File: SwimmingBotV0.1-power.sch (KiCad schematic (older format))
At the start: 17 parts, among them U1 LT3470A, U10 TPS6216X

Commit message: hoh, working on power stuffs now
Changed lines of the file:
@@
 $Descr A4 11693 8268
 encoding utf-8
-Sheet 3 8
+Sheet 2 8
 Title ""
 Date ""
@@
 P 7850 3950
 F 0 "L1" V 7800 3950 50  0000 C CNN
-F 1 "10uH Isat 400mA" V 7950 3950 50  0000 C CNN
+F 1 "10uH Isat 400mA" V 7800 4400 50  0000 C CNN
 F 2 "Resistors_SMD:R_1210" H 7850 3950 50  0001 C CNN
 F 3 "" H 7850 3950 50  0000 C CNN
@@
 P 7500 4150
 F 0 "C40" H 7400 4250 50  0000 L CNN
-F 1 "100nF" H 7525 4050 50  0000 L CNN
+F 1 "100nF" H 7300 4050 50  0000 L CNN
 F 2 "Capacitors_SMD:C_0402" H 7538 4000 50  0001 C CNN
 F 3 "" H 7500 4150 50  0000 C CNN

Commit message: not final, moving towards board v0.2
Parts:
- added R?: 10k, Resistors_SMD:R_0402, symbol R
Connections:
- net 1S: now also R?.1
- net PROC_3.3V_EN: now also R?.2
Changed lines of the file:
@@
 $EndComp
-Wire Wire Line
-	6150 4200 6050 4200
-Wire Wire Line
-	6050 4200 6050 3850
-Connection ~ 6050 3850
 Wire Wire Line
 	6150 4100 5950 4100
@@
 	5950 4100 5950 5000
 Connection ~ 5950 5000
-Wire Wire Line
-	6150 4400 6100 4400
-Text HLabel 6100 4400 0    60   Input ~ 0
+Text HLabel 6000 4600 0    60   Input ~ 0
 PROC_3.3V_EN
 $Comp
@@
 $EndComp
 Wire Wire Line
-	6700 1800 5850 1800
+	5850 1800 6700 1800
 Wire Wire Line
 	6450 2100 5850 2100
@@
 	1    0    0    -1
 $EndComp
+$Comp
+L R R?
+U 1 1 57477723
+P 6300 4600
+F 0 "R?" V 6380 4600 50  0000 C CNN
+F 1 "10k" V 6300 4600 50  0000 C CNN
+F 2 "Resistors_SMD:R_0402" V 6230 4600 50  0001 C CNN
+F 3 "" H 6300 4600 50  0000 C CNN
+	1    6300 4600
+	0    1    1    0
+$EndComp
+Wire Wire Line
+	6150 4600 6150 4400
+Text Label 6450 4600 0    60   ~ 0
+1S
+Wire Wire Line
+	6000 4600 6150 4600
+Connection ~ 6150 4600
+Wire Wire Line
+	6150 4200 6050 4200
+Wire Wire Line
+	6050 4200 6050 3850
 $EndSCHEMATC

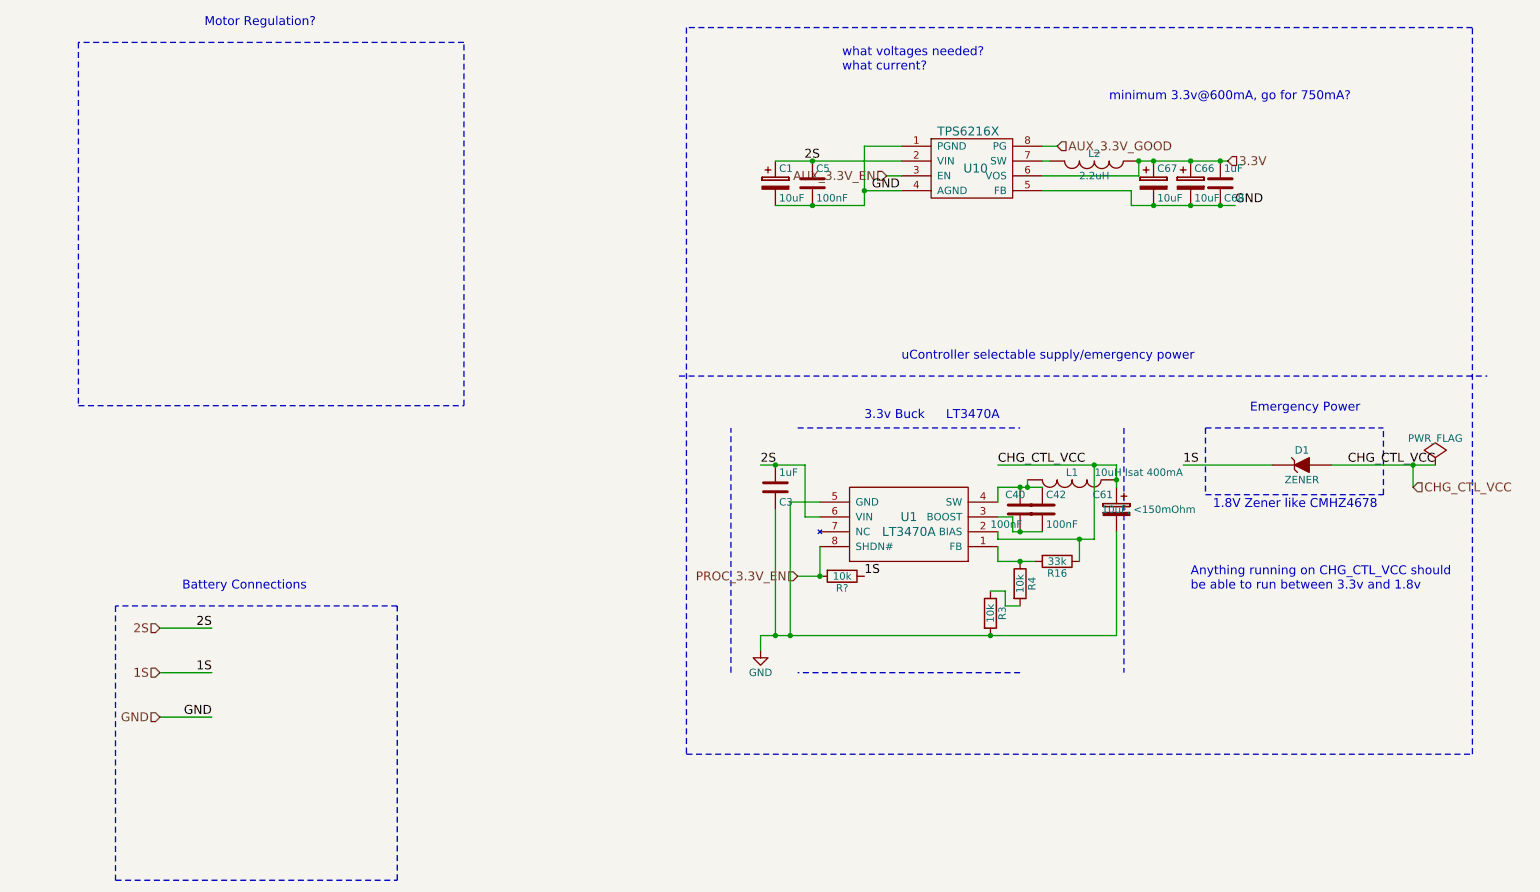
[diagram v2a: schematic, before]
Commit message: potentially done with parts removal and reselection, on to pcb layout
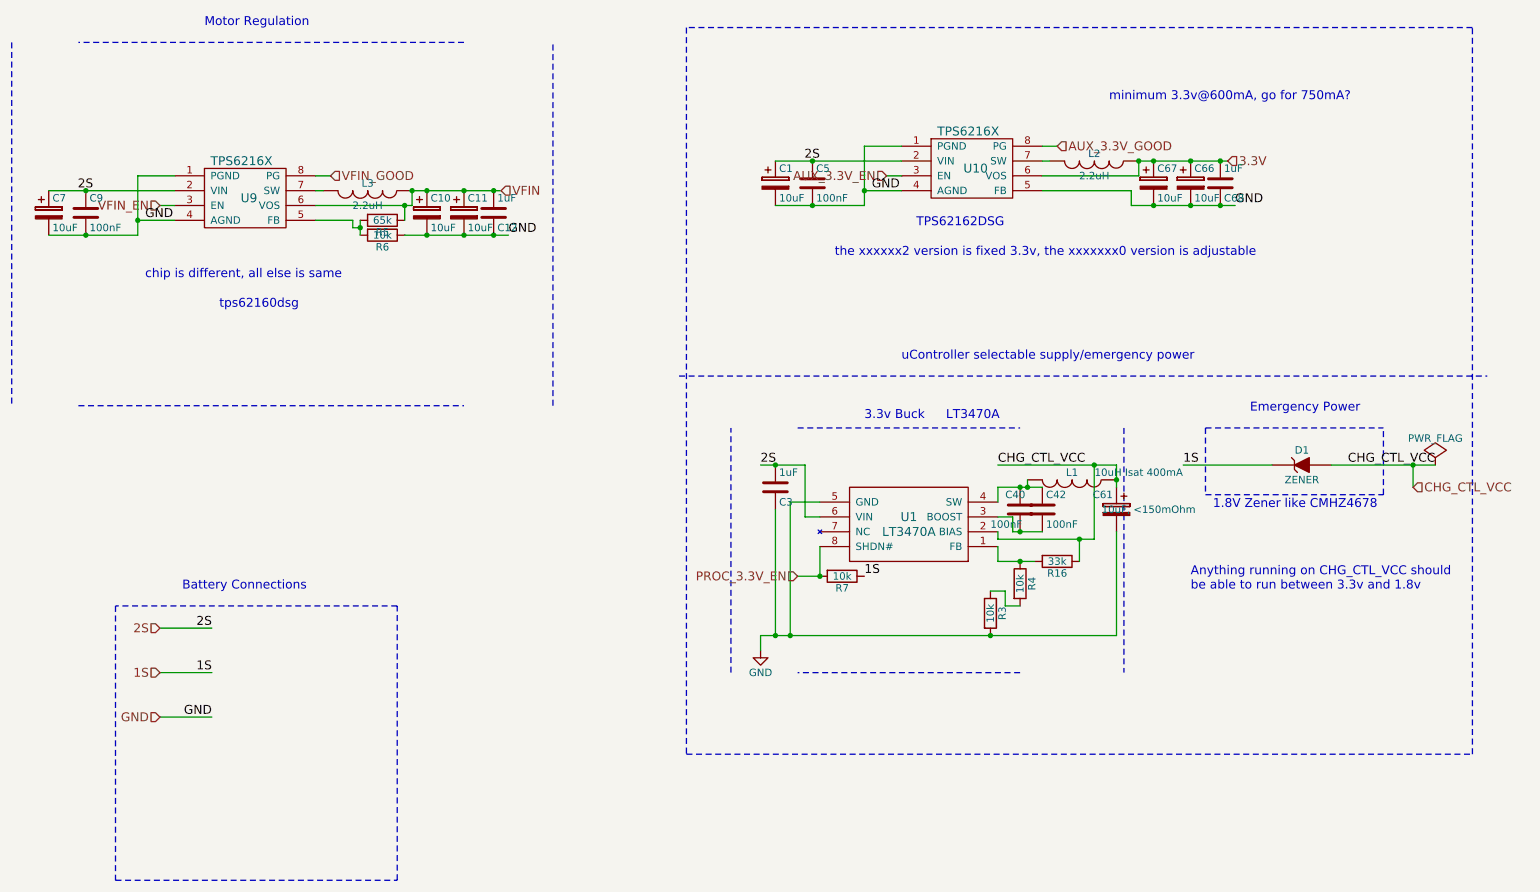
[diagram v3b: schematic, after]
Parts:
- added C10, C11, C7: 10uF, Capacitors_Tantalum_SMD:TantalC_SizeB_EIA-3528_HandSoldering, symbol CP
- added C12: 1uF, Capacitors_SMD:C_0402, symbol C
- added C9: 100nF, Capacitors_SMD:C_0402, symbol C
- added L3: 2.2uH, Inductors:NR4018, symbol INDUCTOR
- added R5: 65k, symbol R
- added R6: 10k, symbol R
- added U9: TPS6216X, Custom_Footprints:WSON-8, symbol TPS6216X
- gave numbers to parts that had none: 1
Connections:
- net 2S: now also C7.1, C9.1, U9.2 (VIN)
- net GND: now also C10.2, C11.2, C12.1, C7.2, C9.2, R6.1, U9.1 (PGND), U9.4 (AGND)
- new net: R5.2, R6.2, U9.5 (FB)
- new net: L3.2, U9.7 (SW)
- new net VFIN: C10.1, C11.1, C12.2, L3.1, R5.1, U9.6 (VOS)
- new net VFIN_EN: U9.3 (EN)
- new net VFIN_GOOD: U9.8 (PG)
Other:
- note added: "Motor Regulation"
- note added: "TPS62162DSG"
- note added: "chip is different, all else is same"
- note added: "the xxxxxx2 version is fixed 3.3v, the xxxxxxx0 version is adjustable"
- note added: "tps62160dsg"
- note removed: "Motor Regulation?"
- note removed: "what voltages needed?\nwhat current?\n"
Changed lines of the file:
@@
 $EndDescr
 Wire Notes Line
-	1150 1000 1150 3450
+	700  1000 700  3450
 Wire Notes Line
 	1150 3450 3750 3450
 Wire Notes Line
-	3750 3450 3750 1000
+	4350 3450 4350 1000
 Wire Notes Line
 	3750 1000 1150 1000
 Text Notes 2000 900  0    60   ~ 0
-Motor Regulation?
+Motor Regulation
 Wire Notes Line
 	5250 900  5250 5800
@@
 Text Label 2050 4950 2    60   ~ 0
 2S
-Text Notes 6300 1200 0    60   ~ 0
-what voltages needed?\nwhat current?\n
 Text Notes 8100 1400 0    60   ~ 0
 minimum 3.3v@600mA, go for 750mA?
@@
 	7350 3850 8150 3850
 $Comp
-L GND #PWR02
+L GND #PWR2
 U 1 1 575451D8
 P 5750 5100
-F 0 "#PWR02" H 5750 4850 50  0001 C CNN
+F 0 "#PWR2" H 5750 4850 50  0001 C CNN
 F 1 "GND" H 5750 4950 50  0000 C CNN
 F 2 "" H 5750 5100 50  0000 C CNN
@@
 Connection ~ 6100 2100
 $Comp
-L PWR_FLAG #FLG03
+L PWR_FLAG #FLG1
 U 1 1 5759624D
 P 10300 3850
-F 0 "#FLG03" H 10300 3945 50  0001 C CNN
+F 0 "#FLG1" H 10300 3945 50  0001 C CNN
 F 1 "PWR_FLAG" H 10300 4030 50  0000 C CNN
 F 2 "" H 10300 3850 50  0000 C CNN
@@
 $EndComp
 $Comp
-L R R?
+L R R7
 U 1 1 57477723
 P 6300 4600
-F 0 "R?" V 6380 4600 50  0000 C CNN
+F 0 "R7" V 6380 4600 50  0000 C CNN
 F 1 "10k" V 6300 4600 50  0000 C CNN
 F 2 "Resistors_SMD:R_0402" V 6230 4600 50  0001 C CNN
@@
 Wire Wire Line
 	6050 4200 6050 3850
+Text HLabel 4000 2000 2    60   Input ~ 0
+VFIN
+$Comp
+L CP C11
+U 1 1 579CADAB
+P 3750 2150
+F 0 "C11" H 3775 2250 50  0000 L CNN
+F 1 "10uF" H 3775 2050 50  0000 L CNN
+F 2 "Capacitors_Tantalum_SMD:TantalC_SizeB_EIA-3528_HandSoldering" H 3788 2000 50  0001 C CNN
+F 3 "" H 3750 2150 50  0000 C CNN
+	1    3750 2150
+	1    0    0    -1
+$EndComp
+Text Label 4050 2300 0    60   ~ 0
+GND
+$Comp
+L TPS6216X U9
+U 1 1 579CADB2
+P 2300 2050
+F 0 "U9" H 2300 2050 60  0000 C CNN
+F 1 "TPS6216X" H 2250 2300 60  0000 C CNN
+F 2 "Custom_Footprints:WSON-8" H 2300 2050 60  0001 C CNN
+F 3 "" H 2300 2050 60  0000 C CNN
+	1    2300 2050
+	1    0    0    -1
+$EndComp
+$Comp
+L INDUCTOR L3
+U 1 1 579CADB8
+P 3100 2000
+F 0 "L3" V 3050 2000 50  0000 C CNN
+F 1 "2.2uH" V 3200 2000 50  0000 C CNN
+F 2 "Inductors:NR4018" H 3100 2000 50  0001 C CNN
+F 3 "" H 3100 2000 50  0000 C CNN
+	1    3100 2000
+	0    1    1    0
+$EndComp
+Wire Wire Line
+	2800 2000 2750 2000
+Wire Wire Line
+	2750 2100 3400 2100
+Wire Wire Line
+	3400 2100 3400 2000
+Wire Wire Line
+	2750 1900 2850 1900
+Text HLabel 2850 1900 2    60   Input ~ 0
+VFIN_GOOD
+$Comp
+L CP C10
+U 1 1 579CADC3
+P 3500 2150
+F 0 "C10" H 3525 2250 50  0000 L CNN
+F 1 "10uF" H 3525 2050 50  0000 L CNN
+F 2 "Capacitors_Tantalum_SMD:TantalC_SizeB_EIA-3528_HandSoldering" H 3538 2000 50  0001 C CNN
+F 3 "" H 3500 2150 50  0000 C CNN
+	1    3500 2150
+	1    0    0    -1
+$EndComp
+Wire Wire Line
+	3350 2300 4050 2300
+Connection ~ 3750 2300
+Wire Wire Line
+	3400 2000 4000 2000
+Connection ~ 3500 2000
+Connection ~ 3750 2000
+Connection ~ 3400 2000
+$Comp
+L C C12
+U 1 1 579CADCF
+P 3950 2150
+F 0 "C12" H 3975 2250 50  0000 L CNN
+F 1 "1uF" H 3975 2050 50  0000 L CNN
+F 2 "Capacitors_SMD:C_0402" H 3988 2000 50  0001 C CNN
+F 3 "" H 3950 2150 50  0000 C CNN
+	1    3950 2150
+	1    0    0    1
+$EndComp
+Connection ~ 3950 2000
+Connection ~ 3950 2300
+Connection ~ 3500 2300
+Wire Wire Line
+	1800 1900 1550 1900
+Wire Wire Line
+	1550 1900 1550 2300
+Wire Wire Line
+	1550 2200 1800 2200
+Text Label 1600 2200 0    60   ~ 0
+GND
+Text Label 1250 2000 2    60   ~ 0
+2S
+Wire Wire Line
+	1800 2100 1700 2100
+Text HLabel 1700 2100 0    60   Input ~ 0
+VFIN_EN
+$Comp
+L CP C7
+U 1 1 579CADE1
+P 950 2150
+F 0 "C7" H 975 2250 50  0000 L CNN
+F 1 "10uF" H 975 2050 50  0000 L CNN
+F 2 "Capacitors_Tantalum_SMD:TantalC_SizeB_EIA-3528_HandSoldering" H 988 2000 50  0001 C CNN
+F 3 "" H 950 2150 50  0000 C CNN
+	1    950  2150
+	1    0    0    -1
+$EndComp
+Wire Wire Line
+	950  2000 1800 2000
+Wire Wire Line
+	1550 2300 950  2300
+Connection ~ 1550 2200
+$Comp
+L C C9
+U 1 1 579CADEA
+P 1200 2150
+F 0 "C9" H 1225 2250 50  0000 L CNN
+F 1 "100nF" H 1225 2050 50  0000 L CNN
+F 2 "Capacitors_SMD:C_0402" H 1238 2000 50  0001 C CNN
+F 3 "" H 1200 2150 50  0000 C CNN
+	1    1200 2150
+	1    0    0    -1
+$EndComp
+Connection ~ 1200 2000
+Connection ~ 1200 2300
+$Comp
+L R R6
+U 1 1 579CBA98
+P 3200 2300
+F 0 "R6" V 3280 2300 50  0000 C CNN
+F 1 "10k" V 3200 2300 50  0000 C CNN
+F 2 "" V 3130 2300 50  0000 C CNN
+F 3 "" H 3200 2300 50  0000 C CNN
+	1    3200 2300
+	0    1    1    0
+$EndComp
+$Comp
+L R R5
+U 1 1 579CBAF5
+P 3200 2200
+F 0 "R5" V 3280 2200 50  0000 C CNN
+F 1 "65k" V 3200 2200 50  0000 C CNN
+F 2 "" V 3130 2200 50  0000 C CNN
+F 3 "" H 3200 2200 50  0000 C CNN
+	1    3200 2200
+	0    1    1    0
+$EndComp
+Wire Wire Line
+	3350 2100 3350 2200
+Connection ~ 3350 2100
+Wire Wire Line
+	3050 2300 3050 2200
+Wire Wire Line
+	2750 2200 3000 2200
+Wire Wire Line
+	3000 2200 3000 2250
+Wire Wire Line
+	3000 2250 3050 2250
+Connection ~ 3050 2250
+Text Notes 1600 2600 0    60   ~ 0
+chip is different, all else is same
+Text Notes 2100 2800 0    60   ~ 0
+tps62160dsg
+Text Notes 6800 2250 0    60   ~ 0
+TPS62162DSG
+Text Notes 6250 2450 0    60   ~ 0
+the xxxxxx2 version is fixed 3.3v, the xxxxxxx0 version is adjustable
 $EndSCHEMATC

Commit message: pcb started in earnest, footprint changes in schematics, about to rename v0.2 boardfile to v0.1, kicad needs the same filename to have backrefs for net highlighting
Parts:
- R5, R6: footprint (none) -> Resistors_SMD:R_0402
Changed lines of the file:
@@
 	7350 3850 8150 3850
 $Comp
-L GND #PWR2
+L GND #PWR02
 U 1 1 575451D8
 P 5750 5100
-F 0 "#PWR2" H 5750 4850 50  0001 C CNN
+F 0 "#PWR02" H 5750 4850 50  0001 C CNN
 F 1 "GND" H 5750 4950 50  0000 C CNN
 F 2 "" H 5750 5100 50  0000 C CNN
@@
 Connection ~ 6100 2100
 $Comp
-L PWR_FLAG #FLG1
+L PWR_FLAG #FLG03
 U 1 1 5759624D
 P 10300 3850
-F 0 "#FLG1" H 10300 3945 50  0001 C CNN
+F 0 "#FLG03" H 10300 3945 50  0001 C CNN
 F 1 "PWR_FLAG" H 10300 4030 50  0000 C CNN
 F 2 "" H 10300 3850 50  0000 C CNN
@@
 F 0 "R6" V 3280 2300 50  0000 C CNN
 F 1 "10k" V 3200 2300 50  0000 C CNN
-F 2 "" V 3130 2300 50  0000 C CNN
+F 2 "Resistors_SMD:R_0402" V 3130 2300 50  0001 C CNN
 F 3 "" H 3200 2300 50  0000 C CNN
 	1    3200 2300
@@
 F 0 "R5" V 3280 2200 50  0000 C CNN
 F 1 "65k" V 3200 2200 50  0000 C CNN
-F 2 "" V 3130 2200 50  0000 C CNN
+F 2 "Resistors_SMD:R_0402" V 3130 2200 50  0001 C CNN
 F 3 "" H 3200 2200 50  0000 C CNN
 	1    3200 2200
